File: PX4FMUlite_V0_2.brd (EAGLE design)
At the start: 49.1 x 34.9 mm, 148 parts, among them J201 DF13C-6P-1.25V, J202 DF13C-6P-1.25V, J203 DF13C-6P-1.25V, J204 DF13C-6P-1.25V, J301 47346-0001, J302 DF13C-4P-1.25V, J401 DF13C-4P-1.25V, J403 DF13C-7P-1.25V, J404 DF13C-5P-1.25V, J405 DF13C-4P-1.25V, J702 DF13C-3P-1.25V, J801 JST-ZH-3, M3_MOUNT1101 MOUNT-HOLE3.1MM, M3_MOUNT1102 MOUNT-HOLE3.1MM, M3_MOUNT1103 MOUNT-HOLE3.1MM, M3_MOUNT1104 MOUNT-HOLE3.1MM, U1 MPU-6000QFN-24, U101 STM32F4X7VX, U401 MAX3051, U903 74LVC2G240, X101 3.2x2.5 mm / 24 MHz / 15 ppm

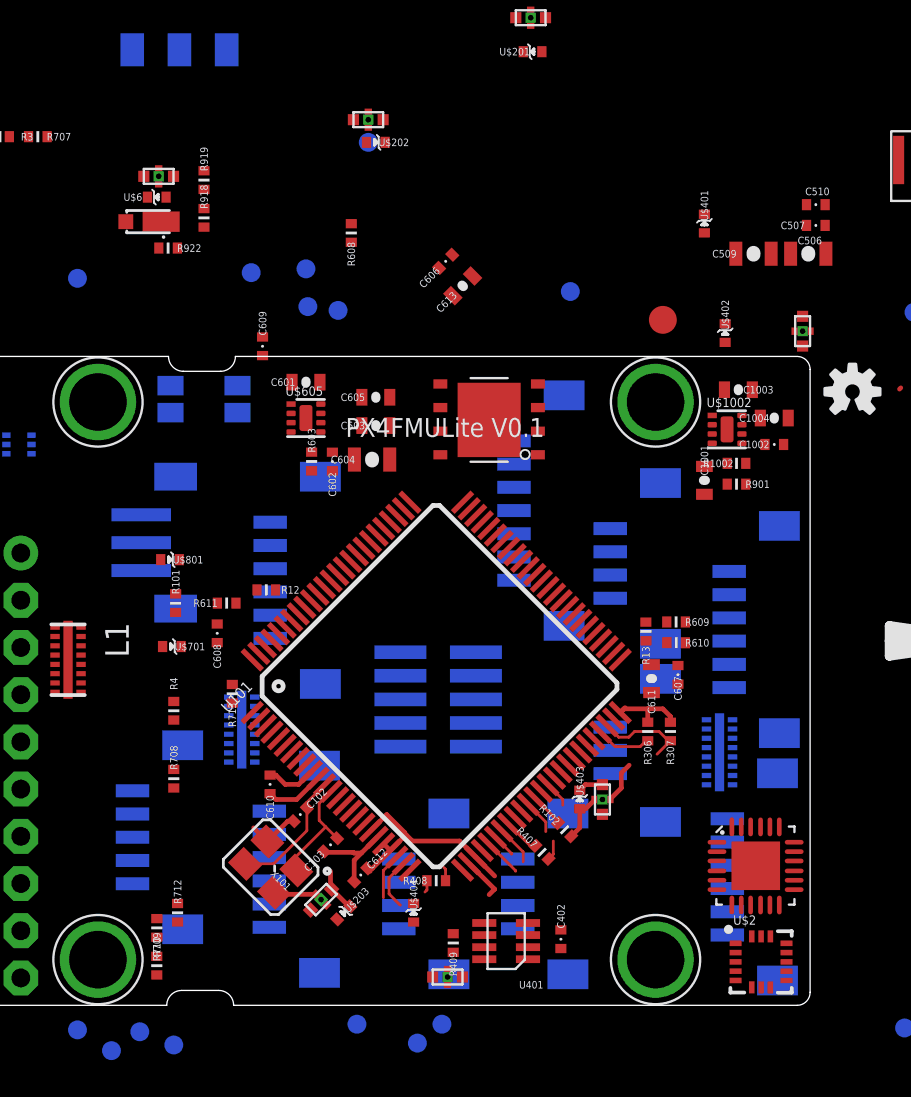
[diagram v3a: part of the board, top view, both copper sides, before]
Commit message: Removed excess UART4/5 connector
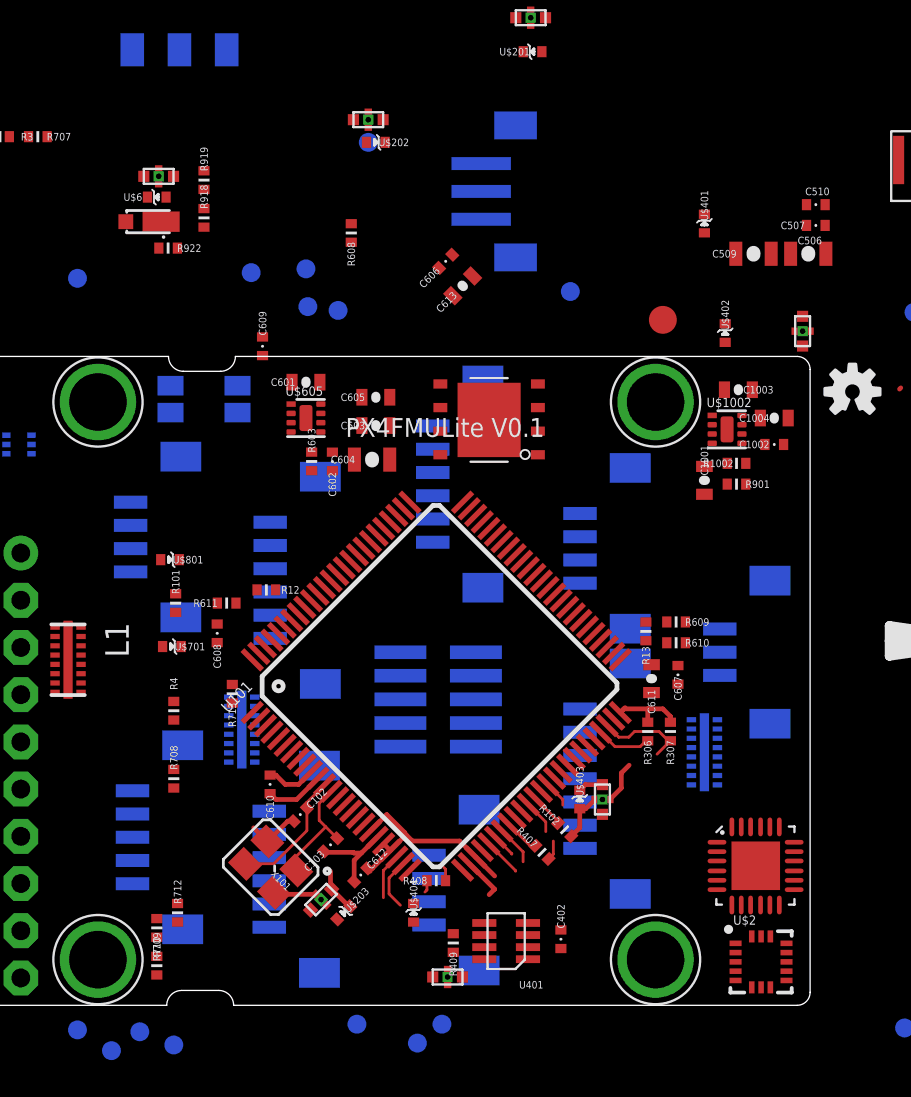
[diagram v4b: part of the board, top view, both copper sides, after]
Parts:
- removed J204: DF13C-6P-1.25V, con-hirose-df13:DF13C-6P-1.25V
- moved J801 26.3 mm to (42.4, 46.5)
- moved J302 25.8 mm to (22.7, 27.9)
- moved J405 21.0 mm to (46.8, 27.3)
- moved J203 17.8 mm to (38.9, 30.8)
- moved J403 14.9 mm to (46.8, 14.9)
- moved J702 7.91 mm to (54.4, 21.7)
- moved J401 4.78 mm to (38.7, 8.94)
- moved L3 0.81 mm to (52.6, 16.4)
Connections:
- net GNDX: no longer J204.P$6
- net N$100: no longer J204.P$1
- net SERIAL4_RX: no longer J204.P$3
- net SERIAL4_TX: no longer J204.P$2
- net SERIAL5_RX: no longer J204.P$5
- net SERIAL5_TX: no longer J204.P$4
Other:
- board text removed: "IO ACT"
- board text removed: "IO B/E"
- board text removed: "IO PWR"

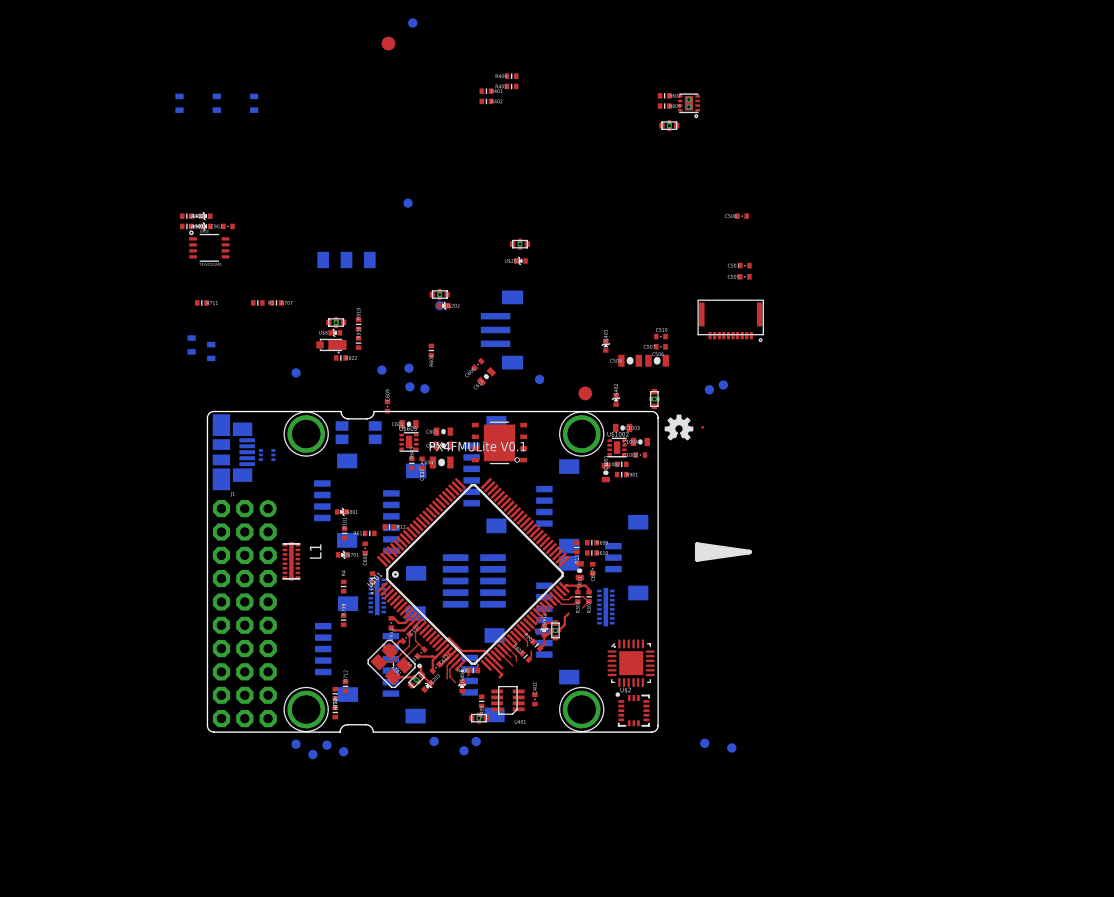
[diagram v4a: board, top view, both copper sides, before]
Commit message: I2C2 connector added.
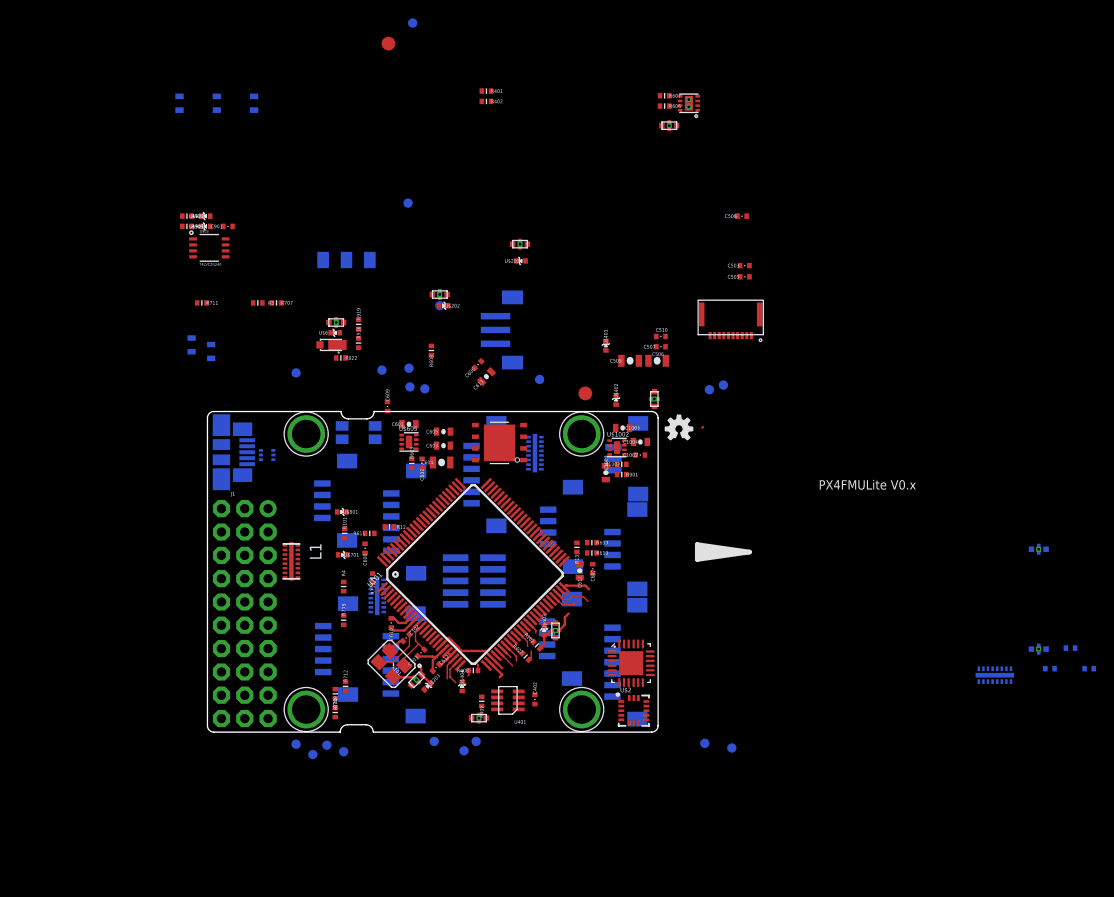
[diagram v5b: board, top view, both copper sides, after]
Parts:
- removed J702: DF13C-3P-1.25V, con-hirose-df13:DF13C-3P-1.25V
- removed R306, R307: 1K5, pixhawk2:0402-RES
- removed R404, R405: 120R, pixhawk2:0402-RES
- added J2: DF13-4P-1.25V, con-hirose-df13:DF13C-4P-1.25V
- added J802: DF13C-3P-1.25V, con-hirose-df13:DF13C-3P-1.25V
- added L4, L5: KNH16C104DA5TS, pixhawk2:KYOCERA-KNH16-DA
- added L6: NUF8402MN, PX4lite:DFN16-THIN
- added R1, R2: 1K5, pixhawk2:0402-RES
- added U$4: PESD0402-140, pixhawk2:0402-TVS
- moved L3 18.5 mm to (44.9, 33.1)
- moved J401 9.32 mm to (47.1, 12.9)
- moved J405 8.77 mm to (54.3, 22.7)
- moved J403 8.71 mm to (54.3, 10.4)
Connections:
- new net N$20: J2.P$3, L6.P$15
- new net N$21: J2.P$1, L5.P$2, U$4.C
- new net N$4: J2.P$2, L6.P$16
- net FMU-I2C1_SCL: now also L6.P$3; no longer R404.P$1
- net FMU-I2C1_SDA: now also L6.P$4; no longer R405.P$1
- net FMU-I2C2_SCL: now also L6.P$1, R1.P$1; no longer R306.P$1
- net FMU-I2C2_SDA: now also L6.P$2, R2.P$1; no longer R307.P$1
- net FMU-VDD_3V3: now also R1.P$2, R2.P$2; no longer R306.P$2, R307.P$2
- net GND: now also J2.P$4, L5.P$3, L5.P$4, L5.P$5, U$4.A
- net GNDX: now also L4.P$3, L4.P$4, L4.P$5, L6.P$EP
- net IO-VDD_3V3: now also J802.P$1; no longer J702.P$1
- net N$33: now also L6.P$14; no longer R404.P$2
- net N$37: now also L6.P$13; no longer R405.P$2
- net N$42: now also L4.P$2
- net N$57: now also J802.P$2; no longer J702.P$2
- net SAFETY: now also J802.P$3; no longer J702.P$3
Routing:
- net FMU-I2C2_SDA: track 5.01 -> 3.89 mm
- net FMU-VDD_3V3: track 19.6 -> 18.6 mm
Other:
- board text added: "AUX ADC"
- board text added: "I2C1"
- board text added: "I2C2"
- board text added: "PX4FMULite V0.x"
- board text added: "SAFETY"
- board text added: "UART1"
- board text added: "UART2"
- board text added: "UART3 / GPS"
- board text removed: "I2C"
- board text removed: "PX4FMU 2.3"
- board text removed: "PX4FMULite V0.1"

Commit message: General shuffling of filters
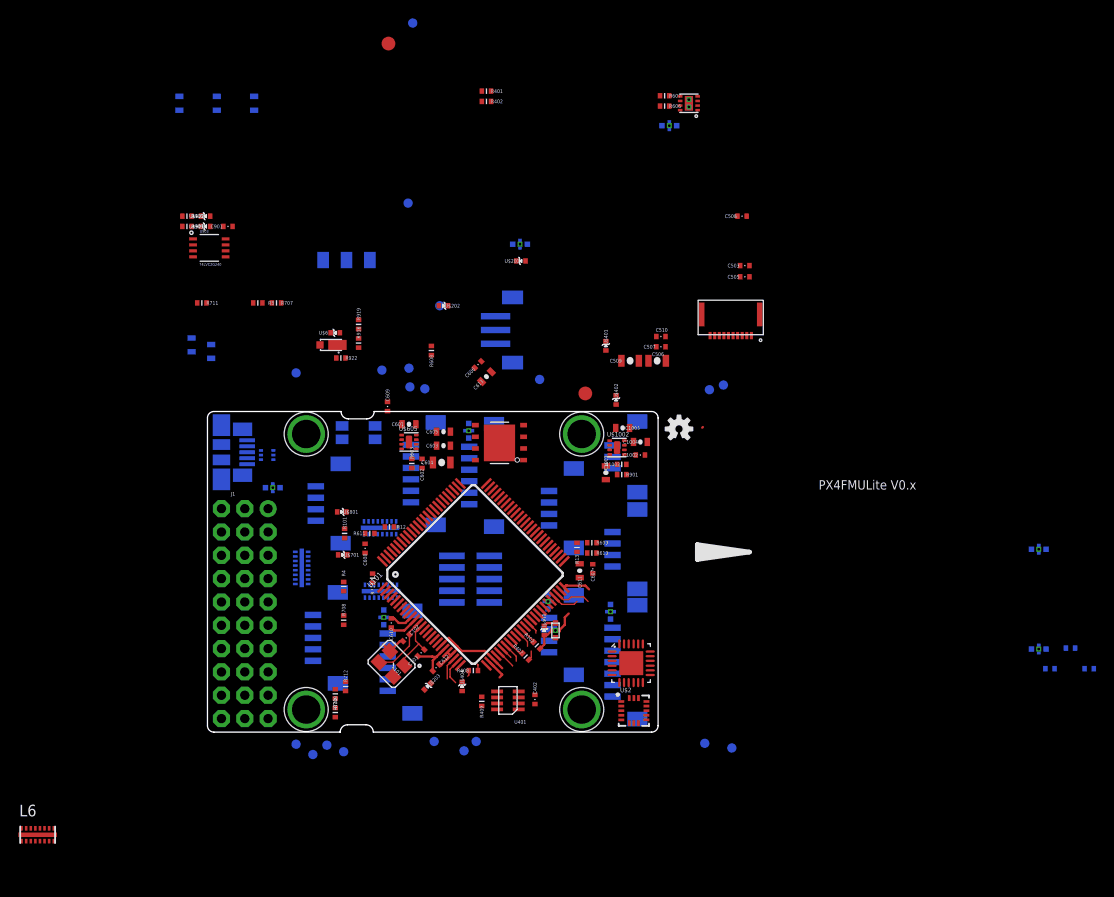
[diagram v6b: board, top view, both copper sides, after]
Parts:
- moved L6 105.7 mm to (-9.25, -8.43), flipped to the top
- moved L402 23.7 mm to (53.1, 15.8), flipped to the bottom, turned to 270 degrees
- moved L3 22.5 mm to (28.1, 18.1), turned to 180 degrees
- moved J203 22.4 mm to (29.8, 10.4)
- moved J202 22.3 mm to (38.7, 30.7)
- moved L901 19.3 mm to (16.4, 29.4), flipped to the bottom
- moved L202 15.2 mm to (37.7, 35.6), flipped to the bottom, turned to 270 degrees
- moved L403 14.8 mm to (46.3, 17.0), flipped to the bottom, turned to 270 degrees
- moved J401 12.1 mm to (54.3, 22.7)
- moved J405 11.6 mm to (47.3, 13.3)
- moved L203 7.68 mm to (28.4, 15.2), flipped to the bottom, turned to 270 degrees
- moved L2 7.42 mm to (28.0, 25.0), turned to 0 degrees
- moved J201 5.70 mm to (32.3, 30.9)
- moved J2 2.03 mm to (47.3, 27.1)
- moved J404 1.65 mm to (21.6, 13.0)
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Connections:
- new net N$22: J405.P$3, L6.P$11
- new net N$24: J405.P$2, L6.P$12
- net CAN_H: now also L6.P$5; no longer J405.P$2
- net CAN_L: now also L6.P$6; no longer J405.P$3
- net FMU-VDD_5V: now also LED701.A, LED704.A
- net VDD_5V_IN: no longer LED701.A, LED704.A
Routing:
- net GNDX: track 21.4 -> 18.8 mm
- net N$100: track 2.37 -> 0.00 mm

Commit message: USB connector move to side. UART conns together
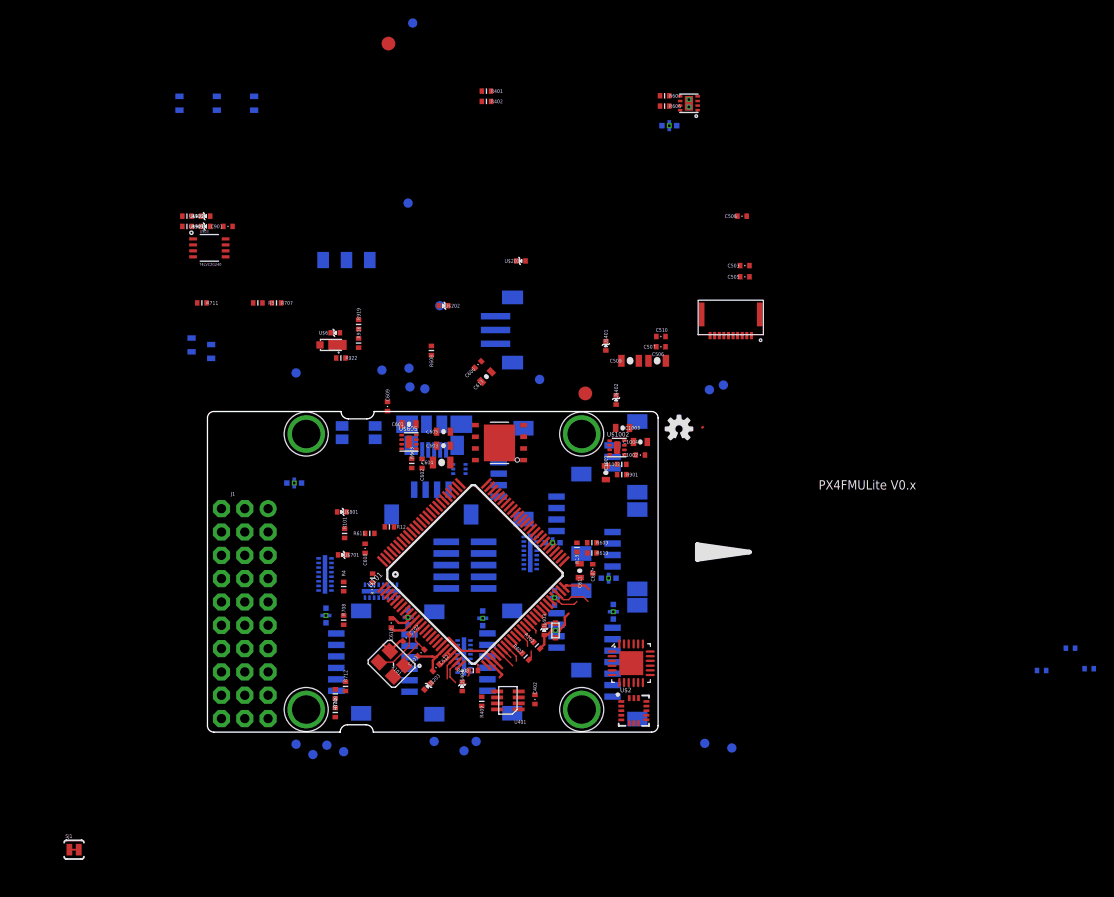
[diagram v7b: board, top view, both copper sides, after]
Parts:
- added SJ1: SOLDERJUMPERTRACE, SparkFun-Passives:SJ_2S-TRACE
- moved L6 61.8 mm to (44.4, 22.3), flipped to the bottom, turned to 270 degrees
- moved L5 54.2 mm to (46.8, 23.4), turned to 180 degrees
- moved L4 46.9 mm to (52.9, 19.5), turned to 180 degrees
- moved L201 42.4 mm to (31.1, 15.2), turned to 270 degrees
- moved J404 27.0 mm to (41.9, 30.9)
- moved J301 23.4 mm to (33.9, 36.3), turned to 270 degrees
- moved J201 22.1 mm to (40.6, 10.4)
- moved J202 21.4 mm to (32.2, 10.3)
- moved U$301 21.0 mm to (36.7, 31.4)
- moved L202 20.5 mm to (39.2, 15.1)
- moved L2 16.7 mm to (37.2, 11.0), turned to 270 degrees
- moved J302 11.7 mm to (33.6, 28.2), turned to 0 degrees
- moved L203 6.30 mm to (22.1, 15.4)
- moved J203 5.59 mm to (24.2, 10.4)
- moved L1 2.64 mm to (22.0, 19.9), turned to 90 degrees
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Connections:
- removed net N$24: J405.P$2, L6.P$12
- net CAN_H: now also J405.P$2; no longer L6.P$5
- net CAN_L: now also J405.P$3, SJ1.2; no longer L6.P$6, R409.P$2
- net FMU-CH1: now also L1.P$1
- net FMU-CH2: now also L1.P$2
- net FMU-CH3: now also L1.P$3
- net FMU-CH4: now also L1.P$4
- net FMU-CH5: now also L1.P$5
- net FMU-CH8: now also L1.P$6
- net GND: now also L1.P$EP, L2.P$EP, L3.P$EP
- net GNDX: no longer L1.P$EP, L2.P$EP, L3.P$EP
- net N$16: now also L1.P$10
- net N$22: now also R409.P$2, SJ1.1; no longer J405.P$3, L6.P$11
- net N$68: now also L1.P$12
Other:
- board text removed: "BUZZER"
- board text removed: "FMU PWR"
- board text removed: "SWITCH"

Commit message: Tweaks on MPU6000
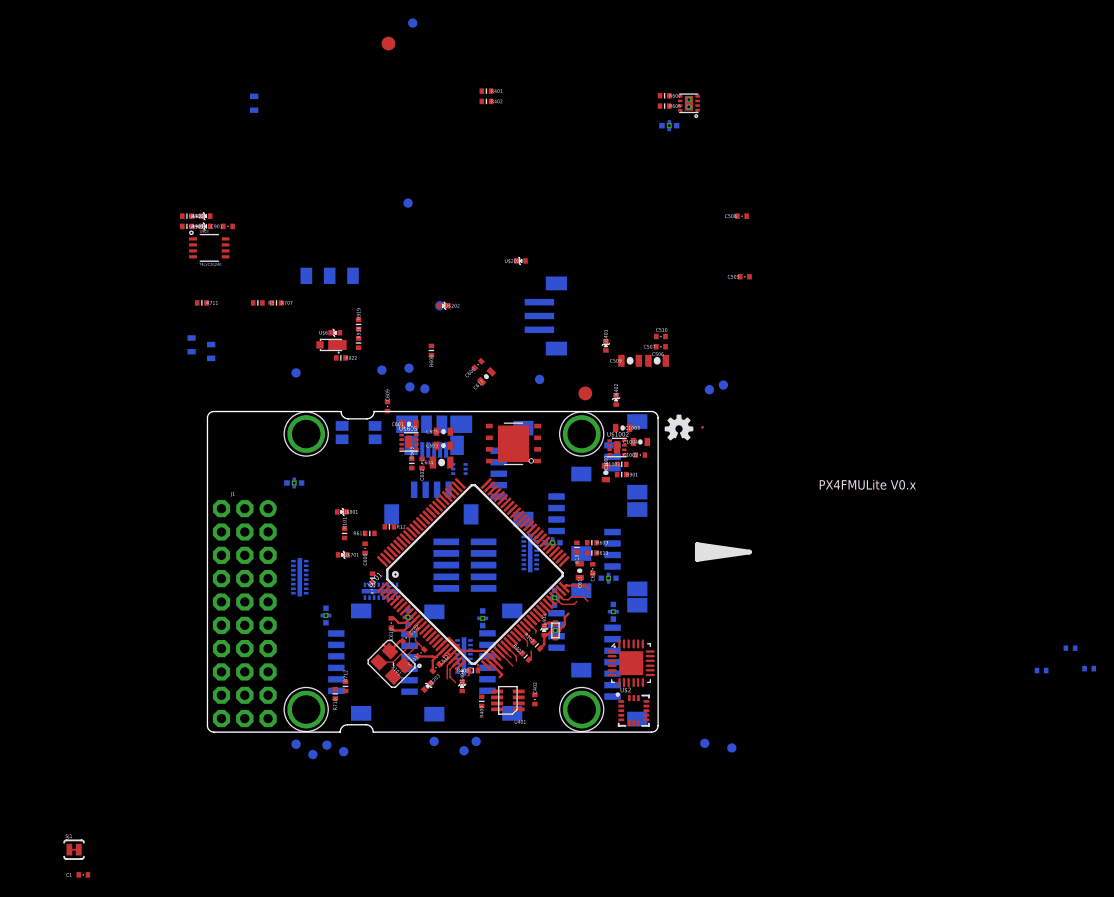
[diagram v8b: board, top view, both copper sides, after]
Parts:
- removed C503: 0u1, pixhawk2:0402-CAP
- removed LED702: GREEN, pixhawk2:0603-LED
- removed LED703: AMBER, pixhawk2:0603-LED
- removed R4, R708, R709: 220R, pixhawk2:0402-RES
- removed U$1: 0512811094, pixhawk2:51281-1094
- added C1: 10n, pixhawk2:0402-CAP
- moved J801 5.01 mm to (47.1, 48.1)
- moved L1 2.76 mm to (19.3, 19.6), turned to 270 degrees
- moved JX801 2.52 mm to (22.6, 52.4)
- moved U$3 1.53 mm to (42.6, 34.1)
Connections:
- net !IO-LED_BLUE renamed FMU-LED_BLUE
- net !IO-LED_SAFETY renamed FMU-LED_SAFETY
- removed net !IO-LED_AMBER: R709.P$1
- removed net N$29: LED702.C, R708.P$2
- removed net N$30: C505.P$1
- removed net N$39: R4.P$1, R709.P$2
- removed net N$40: LED703.C, R4.P$2
- new net N$24: LED705.A
- new net N$25: C505.P$1, U1.20
- new net N$27: C1.P$1, U1.10
- net !ACCEL_MAG_CS: no longer U$1.6
- net !GYRO_CS: now also U1.8; no longer U$1.7
- net ACCEL_DRDY: no longer U$1.3
- net FMU-VDD_3V3: now also J802.P$1, U$701.C
- net FMU-VDD_5V: no longer LED702.A, LED703.A, LED705.A
- net GND: now also C1.P$2
- net GNDX: now also U1.1, U1.11, U1.18; no longer C503.P$2, R708.P$1, U$1.2
- net GYRO_DRDY: now also U1.12; no longer U$1.5
- net IO-VDD_3V3: no longer J802.P$1, U$701.C
- net MAG_DRDY: no longer U$1.4
- net SPI_INT_MISO: now also U1.9; no longer U$1.9
- net SPI_INT_MOSI: now also U1.24; no longer U$1.8
- net SPI_INT_SCK: now also U1.23; no longer U$1.10
- net VDD_3V3_SENSORS: now also U1.13; no longer C503.P$1, U$1.1
